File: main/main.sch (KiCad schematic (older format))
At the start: 3 parts, among them J2 AudioJack3, J3 Conn_02x10_Odd_Even

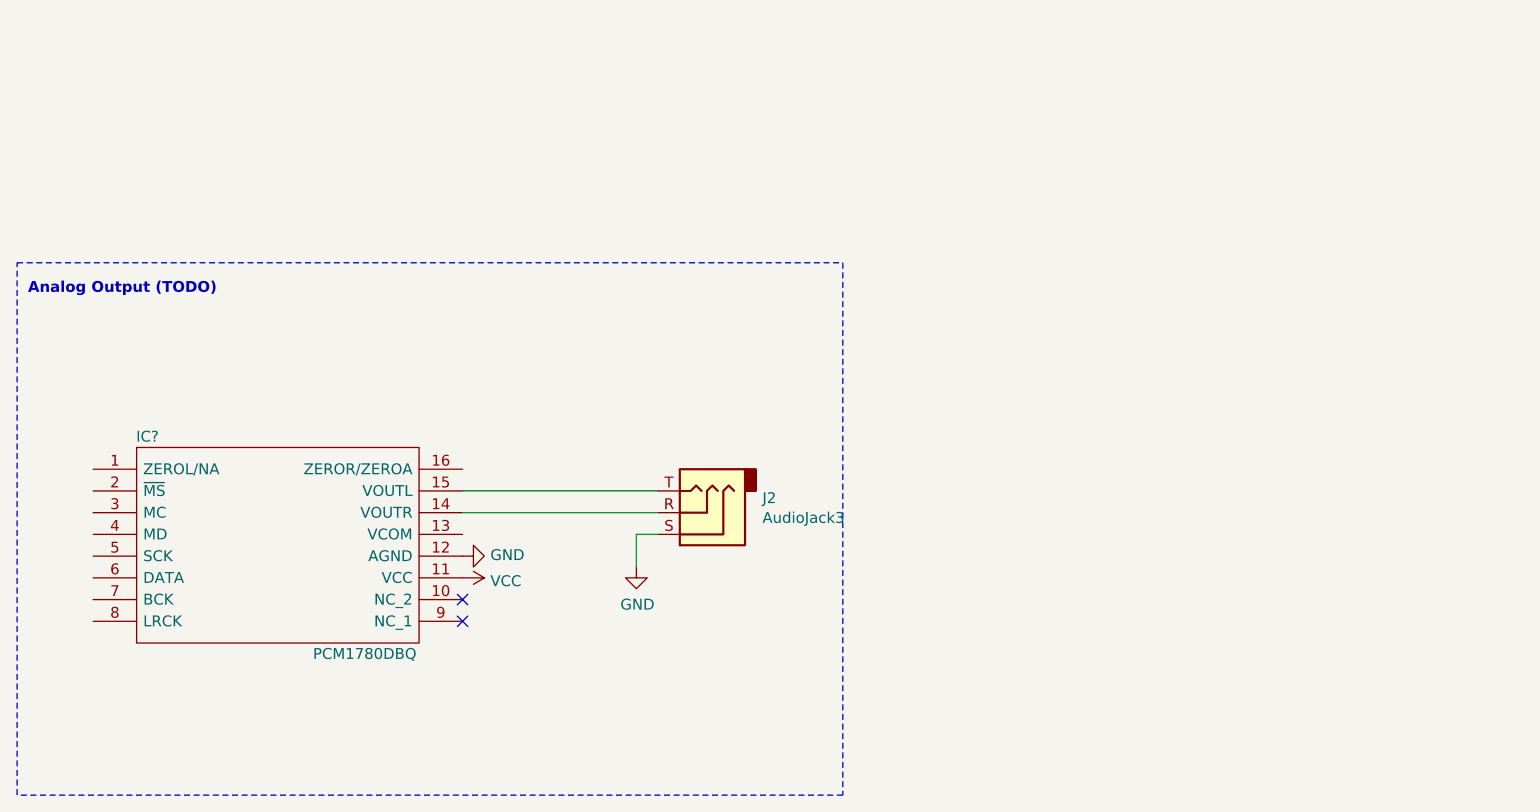
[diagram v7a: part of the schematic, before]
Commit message: Add hierarichal sheet for FPGA
Not done yet
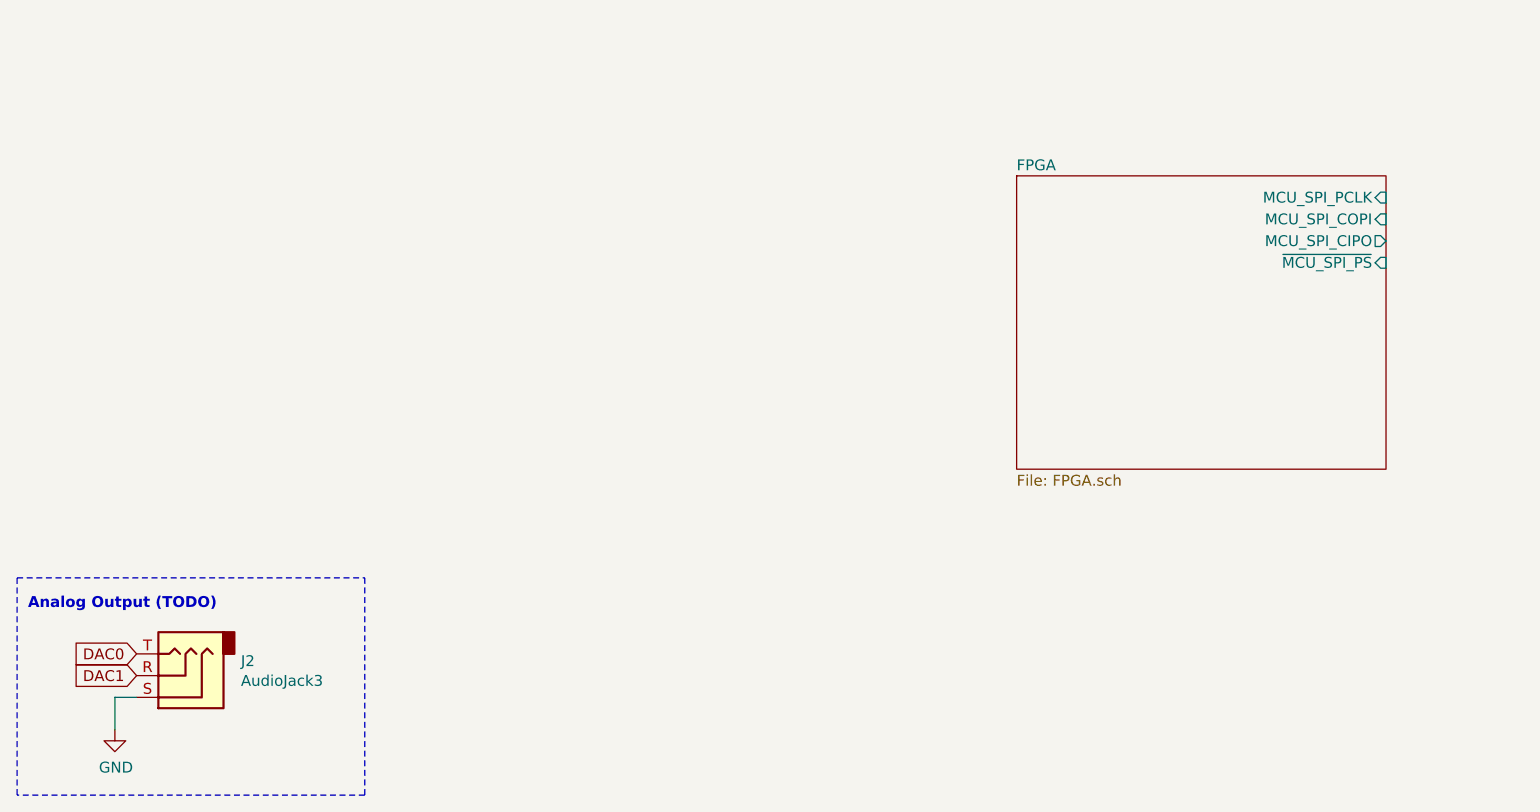
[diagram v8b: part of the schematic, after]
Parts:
- removed IC?: PCM1780DBQ, SOP64P600X175-16N, symbol PCM1780DBQ:PCM1780DBQ
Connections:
- net DAC1: now reaches J2.R
- net DAC0: now reaches J2.T
- no-connect marks 8 -> 6
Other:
- moved on the sheet: J2
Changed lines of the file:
@@
 $Descr A4 11693 8268
 encoding utf-8
-Sheet 1 3
+Sheet 1 4
 Title "Synthesizer"
 Date "2021-09-06"
@@
 L Connector:AudioJack3 J2
 U 1 1 61366BDF
-P 3700 6400
-F 0 "J2" H 3420 6333 50  0000 R CNN
-F 1 "AudioJack3" H 3420 6424 50  0000 R CNN
-F 2 "" H 3700 6400 50  0001 C CNN
-F 3 "~" H 3700 6400 50  0001 C CNN
-	1    3700 6400
+P 1300 7150
+F 0 "J2" H 1020 7083 50  0000 R CNN
+F 1 "AudioJack3" H 1020 7174 50  0000 R CNN
+F 2 "" H 1300 7150 50  0001 C CNN
+F 3 "~" H 1300 7150 50  0001 C CNN
+	1    1300 7150
 	-1   0    0    1
 $EndComp
@@
 L power:GND #PWR0101
 U 1 1 61367C82
-P 3400 6650
-F 0 "#PWR0101" H 3400 6400 50  0001 C CNN
-F 1 "GND" H 3405 6477 50  0000 C CNN
-F 2 "" H 3400 6650 50  0001 C CNN
-F 3 "" H 3400 6650 50  0001 C CNN
-	1    3400 6650
+P 1000 7400
+F 0 "#PWR0101" H 1000 7150 50  0001 C CNN
+F 1 "GND" H 1005 7227 50  0000 C CNN
+F 2 "" H 1000 7400 50  0001 C CNN
+F 3 "" H 1000 7400 50  0001 C CNN
+	1    1000 7400
 	1    0    0    -1
 $EndComp
 Wire Wire Line
-	3400 6650 3400 6500
-Wire Wire Line
-	3400 6500 3500 6500
-Wire Notes Line
-	550  5250 4350 5250
-Wire Notes Line
-	4350 7700 550  7700
-Text Notes 600  5400 0    50   ~ 10
+	1000 7400 1000 7250
+Wire Wire Line
+	1000 7250 1100 7250
+Text GLabel 1100 7050 0    50   Input ~ 0
+DAC0
+Text GLabel 1100 7150 0    50   Input ~ 0
+DAC1
+Wire Notes Line
+	550  6700 2150 6700
+Wire Notes Line
+	2150 7700 550  7700
+Text Notes 600  6850 0    50   ~ 10
 Analog Output (TODO)
 Wire Notes Line
-	550  7700 550  5250
+	2150 6700 2150 7700
+Wire Notes Line
+	550  7700 550  6700
 Wire Notes Line
 	11150 550  7200 550
@@
 Wire Wire Line
 	4500 2400 4800 2400
-$Comp
-L power:VCC #PWR?
-U 1 1 613A81F9
-P 2600 6700
-F 0 "#PWR?" H 2600 6550 50  0001 C CNN
-F 1 "VCC" V 2615 6828 50  0000 L CNN
-F 2 "" H 2600 6700 50  0001 C CNN
-F 3 "" H 2600 6700 50  0001 C CNN
-	1    2600 6700
-	0    1    1    0
-$EndComp
-NoConn ~ 2600 6900
-NoConn ~ 2600 6800
-$Comp
-L PCM1780DBQ:PCM1780DBQ IC?
-U 1 1 613A1DD6
-P 900 6200
-F 0 "IC?" H 1150 6350 50  0000 C CNN
-F 1 "PCM1780DBQ" H 2150 5350 50  0000 C CNN
-F 2 "SOP64P600X175-16N" H 2450 6300 50  0001 L CNN
-F 3 "http://www.ti.com/lit/gpn/pcm1780" H 2450 6200 50  0001 L CNN
-F 4 "PCM1780DBQ, Audio DAC Octal 24 bit-, 192ksps Serial, 16-Pin SSOP" H 2450 6100 50  0001 L CNN "Description"
-F 5 "1.75" H 2450 6000 50  0001 L CNN "Height"
-F 6 "Texas Instruments" H 2450 5900 50  0001 L CNN "Manufacturer_Name"
-F 7 "PCM1780DBQ" H 2450 5800 50  0001 L CNN "Manufacturer_Part_Number"
-F 8 "595-PCM1780DBQ" H 2450 5700 50  0001 L CNN "Mouser Part Number"
-F 9 "https://www.mouser.co.uk/ProductDetail/Texas-Instruments/PCM1780DBQ?qs=wgAEGBTxy7ndC3AC4ryJQw%3D%3D" H 2450 5600 50  0001 L CNN "Mouser Price/Stock"
-F 10 "PCM1780DBQ" H 2450 5500 50  0001 L CNN "Arrow Part Number"
-F 11 "https://www.arrow.com/en/products/pcm1780dbq/texas-instruments?region=nac" H 2450 5400 50  0001 L CNN "Arrow Price/Stock"
-	1    900  6200
-	1    0    0    -1
-$EndComp
-Wire Notes Line
-	4350 5250 4350 7700
-Wire Wire Line
-	2600 6400 3500 6400
-Wire Wire Line
-	2600 6300 3500 6300
-$Comp
-L power:GND #PWR?
-U 1 1 613B4268
-P 2600 6600
-F 0 "#PWR?" H 2600 6350 50  0001 C CNN
-F 1 "GND" V 2605 6472 50  0000 R CNN
-F 2 "" H 2600 6600 50  0001 C CNN
-F 3 "" H 2600 6600 50  0001 C CNN
-	1    2600 6600
-	0    -1   -1   0
-$EndComp
+$Sheet
+S 5150 4850 1700 1350
+U 613F0EEF
+F0 "FPGA" 50
+F1 "FPGA.sch" 50
+F2 "MCU_SPI_PCLK" I R 6850 4950 50
+F3 "MCU_SPI_COPI" I R 6850 5050 50
+F4 "MCU_SPI_CIPO" O R 6850 5150 50
+F5 "~MCU_SPI_PS" I R 6850 5250 50
+$EndSheet
 $EndSCHEMATC
